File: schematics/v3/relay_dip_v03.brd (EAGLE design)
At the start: 50 x 50 mm, 51 parts, among them IC1 74HCT04D, IC2 DS2432P

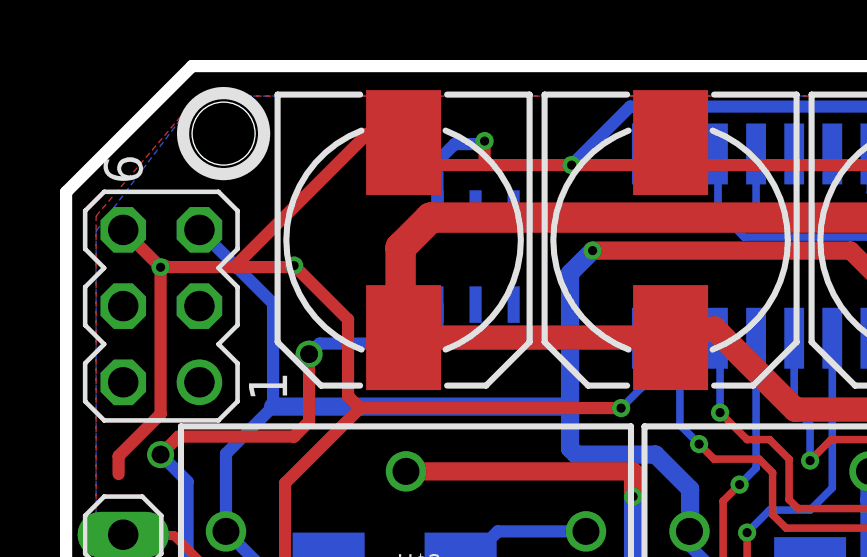
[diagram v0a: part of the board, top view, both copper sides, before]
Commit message: added v3, fixed ds2431 footprint, added quotation
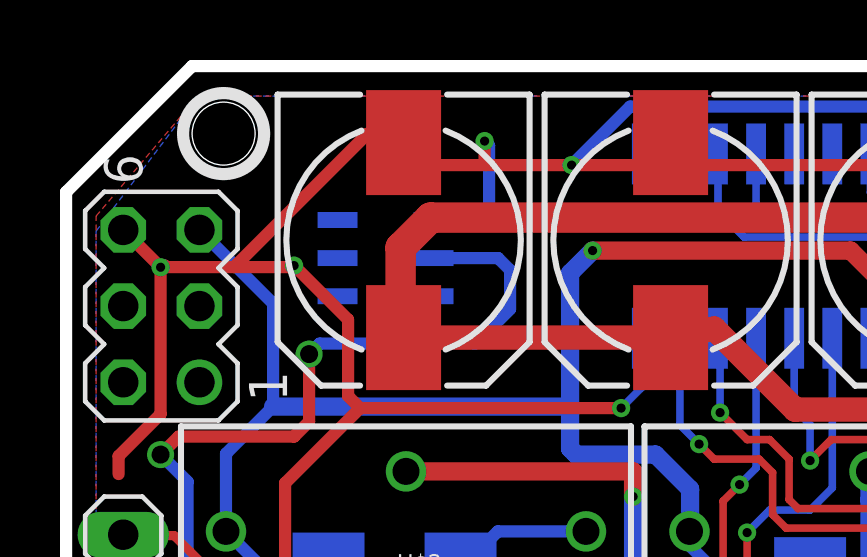
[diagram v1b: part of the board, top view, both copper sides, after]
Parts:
- removed IC2: DS2432P, 1wire:TSOC6
- added U1: DS2431P+T&R, JKW_CHIP:TSOC6
- D1, D2, D3, D4: value (none) -> ES2D
- JP1, JP2, JP3: value (none) -> 571-4-103321-5
- P1, P2, P3, P4: value (none) -> 696-SML-0805ICTR
- POW: value (none) -> 150080BS75000
- R1: value (none) -> 2.2k
- R10, R6, R8, R9: value 10k -> n.a. (10k)
- R2, R3, R4, R5: value 330R -> 200R
- R7: value 330R -> 120R
- S1: value SWITCH-MOMENTARY-2SMD -> n.a.
- SV3: value (none) -> 571-4-146262-1
- SV4: value (none) -> 649-68000-408HLF
- U$1, U$11, U$2, U$8: value RELAYPTH -> SRD-05VDC-SL-C
- U$12, U$3, U$7, U$9: value NMOSFET_SMD_223 -> DMN6068SE-13
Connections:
- new net N$12: IC1.8
- new net N$6: IC1.12
- net 3V: now also IC1.13, IC1.9
- net GND: now also U1.1; no longer IC2.4
- net LD2: now also U1.2; no longer IC2.3
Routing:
- net LD2: track 30.2 -> 35.9 mm
- net GND: track 235.5 -> 236.6 mm

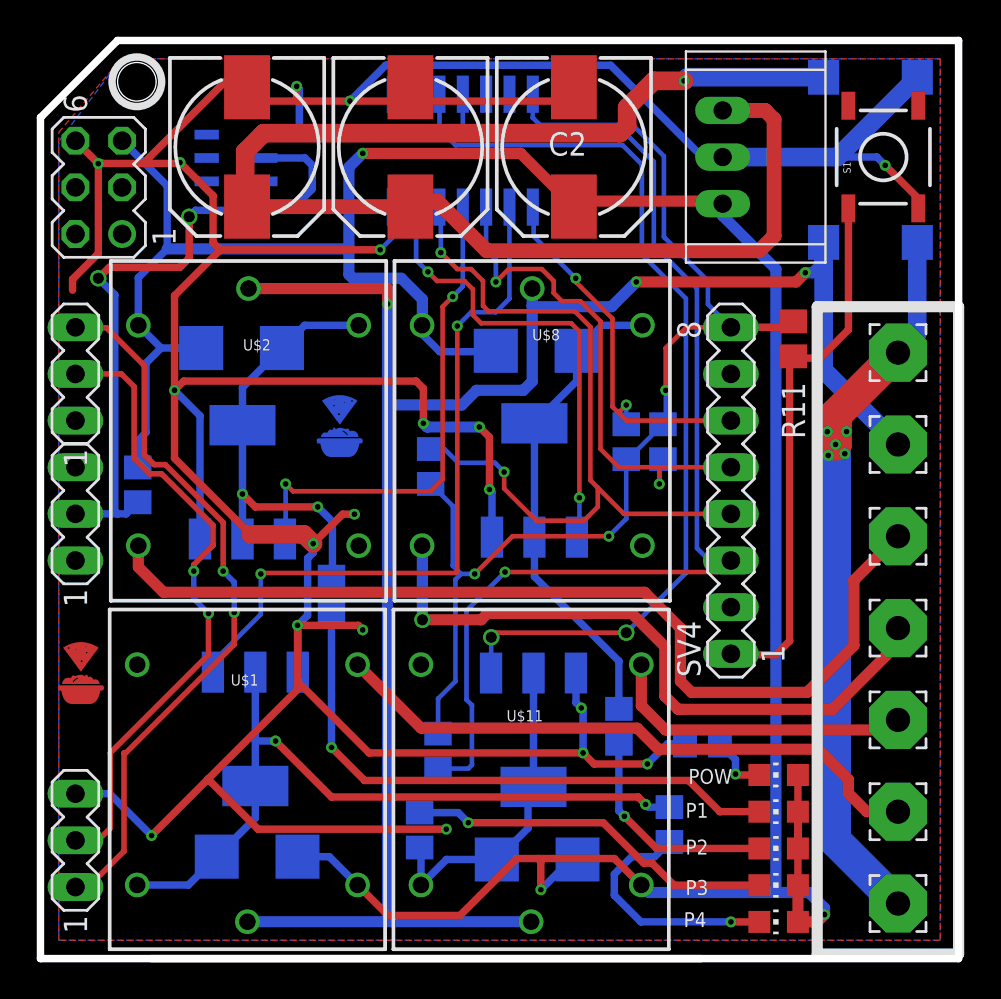
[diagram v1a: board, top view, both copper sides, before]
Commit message: moved relays apart
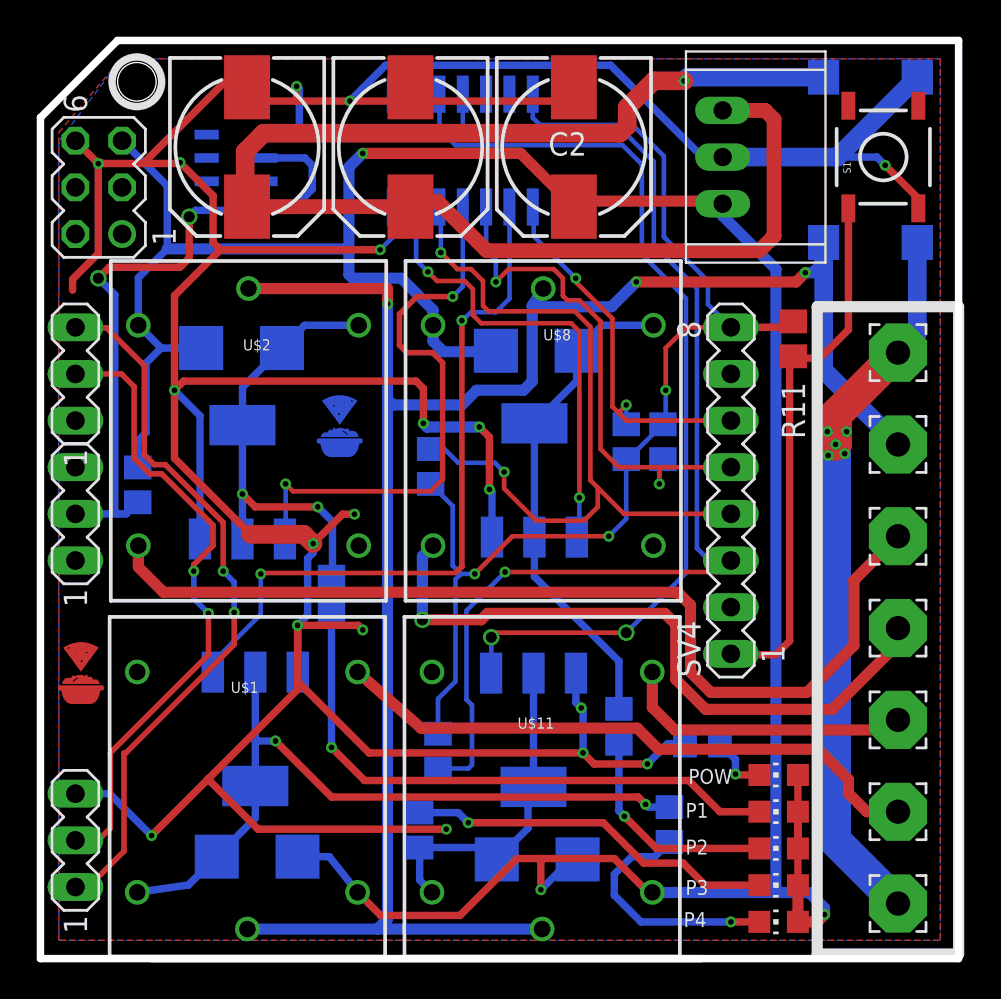
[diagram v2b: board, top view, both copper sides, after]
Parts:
- moved U$11 0.72 mm to (26.7, 9.00)
- moved U$8 0.60 mm to (27.0, 29.1)
- moved U$1 0.40 mm to (10.7, 9.00)
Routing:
- net N$7: track 27.3 -> 31.2 mm
- net PHASE: track 100.7 -> 102.1 mm
- net NCL3: track 17.0 -> 16.0 mm
- net RELAY_LO2: track 26.5 -> 27.1 mm
- net RELAY_LO3: track 18.2 -> 18.8 mm

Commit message: flipped pin header to lower layer
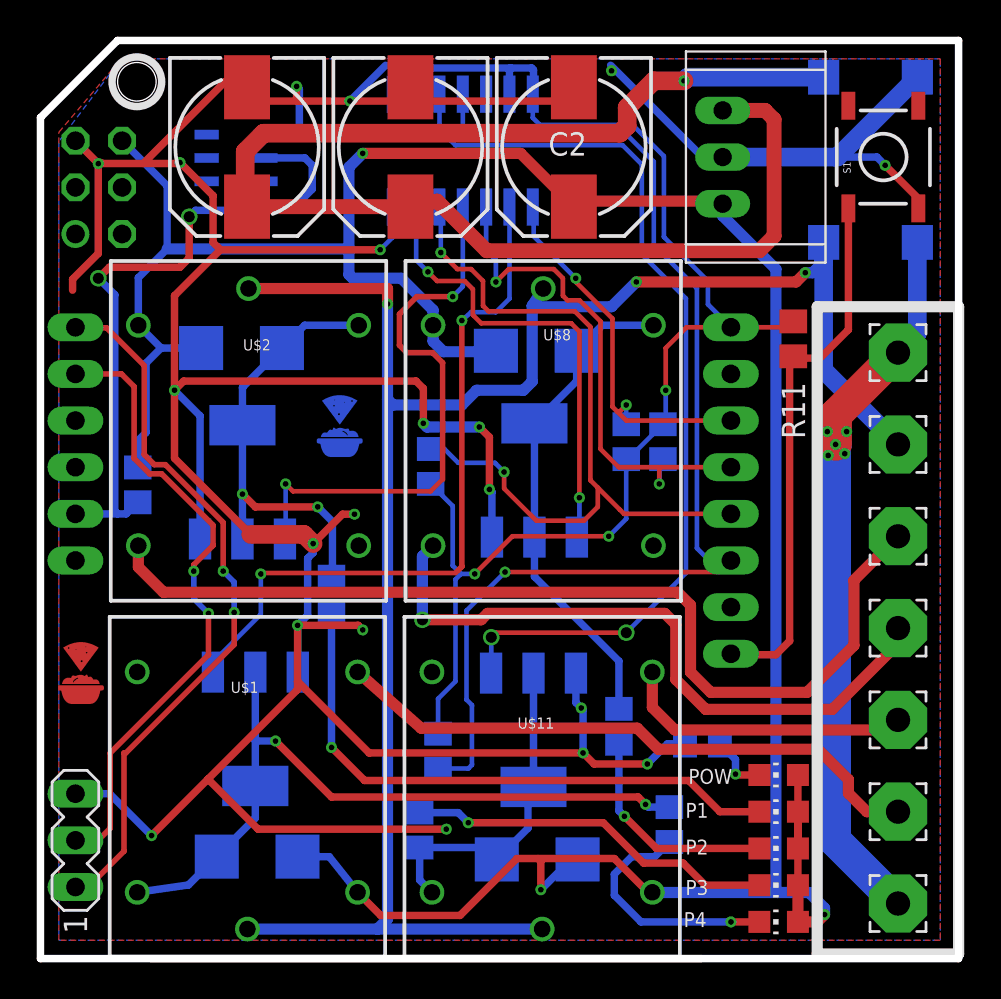
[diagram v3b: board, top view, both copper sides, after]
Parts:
- flipped JP1 to the bottom
- flipped JP2 to the bottom
- flipped SV1 to the bottom
- flipped SV3 to the bottom
- renumbered SV4 to SV1
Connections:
- net GND: now also SV3.5; no longer SV3.6
- net VCC: now also SV3.6; no longer SV3.5
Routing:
- net GND: track 236.6 -> 224.4 mm, vias 19 -> 20
- net 3V: track 63.1 -> 73.6 mm
- net EARTH: track 40.3 -> 43.5 mm

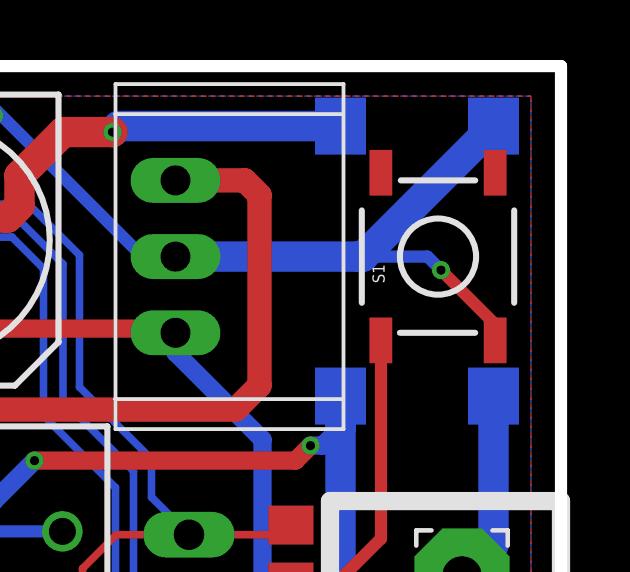
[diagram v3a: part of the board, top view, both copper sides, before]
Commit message: moved switch further outside
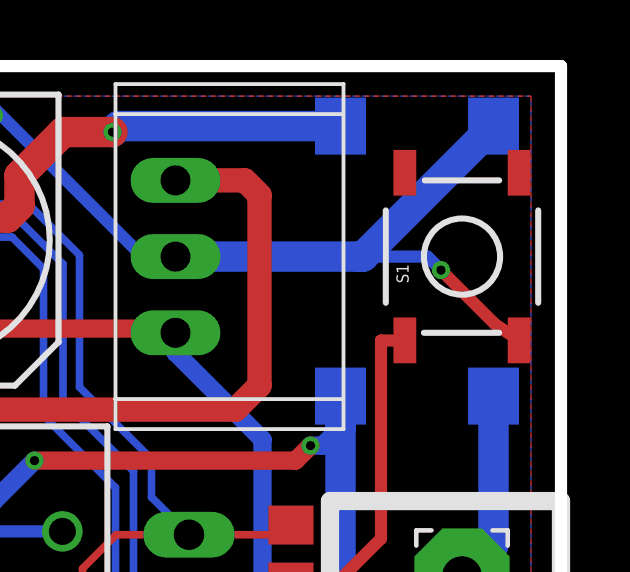
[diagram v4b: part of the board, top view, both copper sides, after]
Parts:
- moved S1 0.80 mm to (46.2, 43.6)
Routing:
- net N$1: track 29.4 -> 30.2 mm

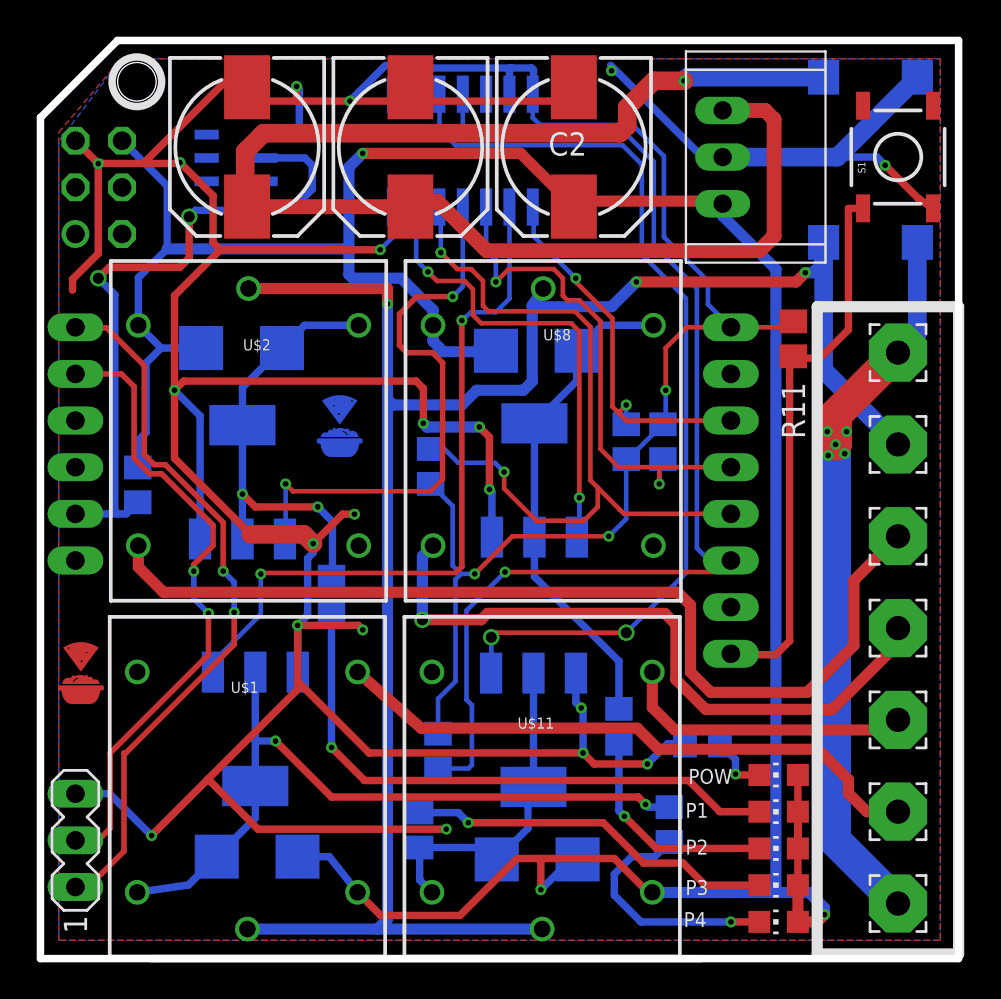
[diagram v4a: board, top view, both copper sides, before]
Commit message: added designators
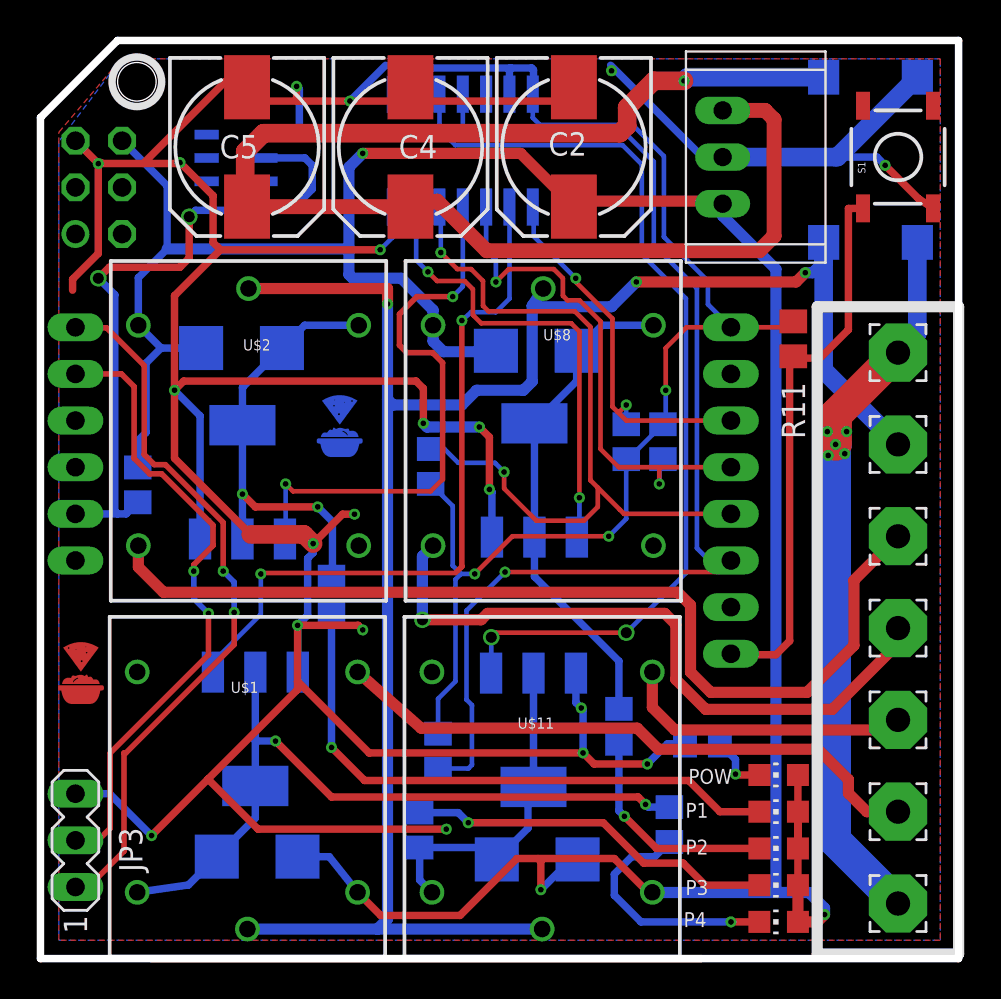
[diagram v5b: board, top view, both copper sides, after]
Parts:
- removed U$5: LOGO_10X10_SILK, logo:LOGO_10X10_SILK
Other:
- board text added: "IOT_STEVE v0.2"
- board text removed: "JKW v0.2"
